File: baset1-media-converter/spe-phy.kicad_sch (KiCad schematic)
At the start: 47 parts, among them J4 CONN_01X02, Q1 SSM6N58NU, U8 DP83TG720S-Q1, U9 ECS-1612MV-250-CN

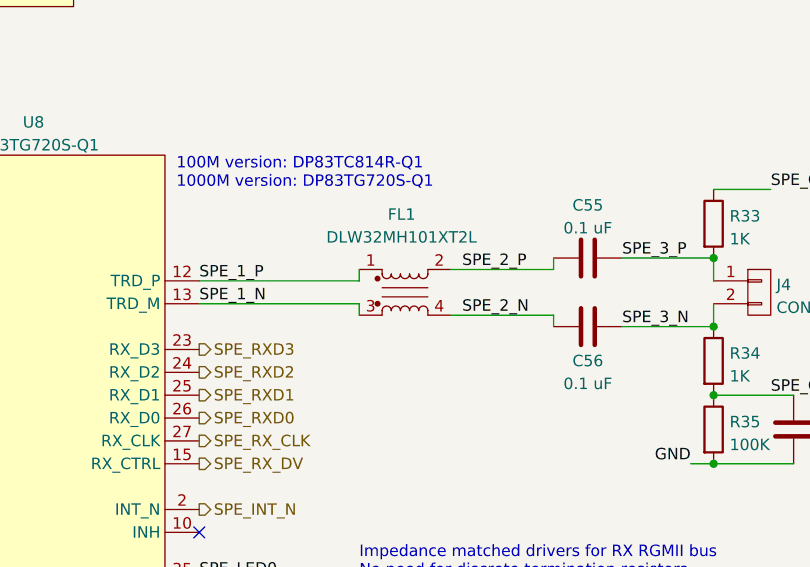
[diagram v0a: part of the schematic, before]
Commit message: Continued layout on media converter
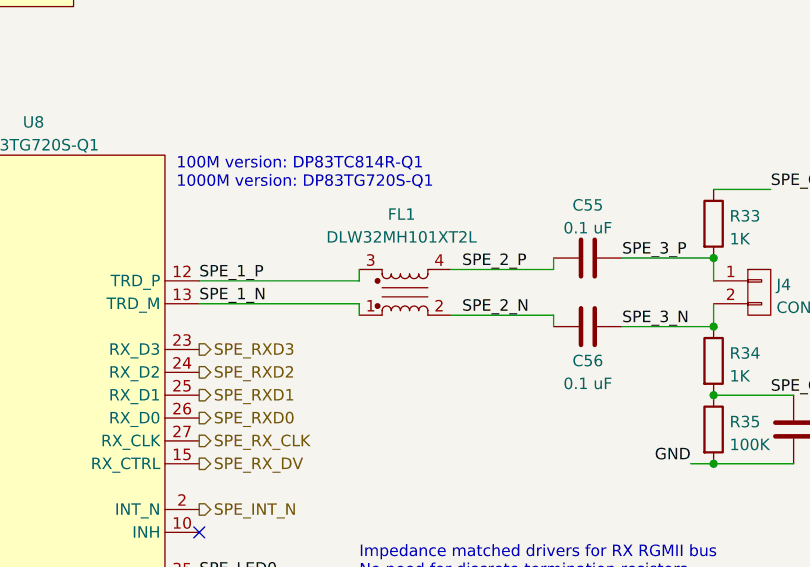
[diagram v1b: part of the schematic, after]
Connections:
- net SPE_1_N: now also FL1.1; no longer FL1.3
- net SPE_1_P: now also FL1.3; no longer FL1.1
- net SPE_2_N: now also FL1.2; no longer FL1.4
- net SPE_2_P: now also FL1.4; no longer FL1.2
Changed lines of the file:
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@@
   (title_block
     (title "BaseT to BaseT1 Media Converter")
-    (date "2024-01-25")
+    (date "2024-01-27")
     (rev "0.1")
     (company "Antikernel Labs")
@@
     (pin "2")
   )
-  (symbol (lib_id "device:EMI_Filter_CommonMode") (at 148.59 68.58 0) (unit 1)
+  (symbol (lib_id "device:EMI_Filter_CommonMode") (at 148.59 68.58 0) (mirror x) (unit 1)
     (in_bom yes) (on_board yes) (fields_autoplaced)
     (property "Reference" "FL1" (id 0) (at 148.209 59.9304 0))
     (property "Value" "DLW32MH101XT2L" (id 1) (at 148.209 62.4673 0))
-    (property "Footprint" "azonenberg_pcb:CMC_1210" (id 2) (at 148.59 67.564 90)
-      (effects (font (size 1.27 1.27)) hide)
-    )
+    (property "Footprint" "azonenberg_pcb:CMC_1210" (id 2) (at 148.59 69.596 90)
+      (effects (font (size 1.27 1.27)) hide)
+    )
